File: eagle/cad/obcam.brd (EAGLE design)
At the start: 64 x 68 mm, 15 parts, among them IC1 NJM2391, IC2 TJ8S06M3L

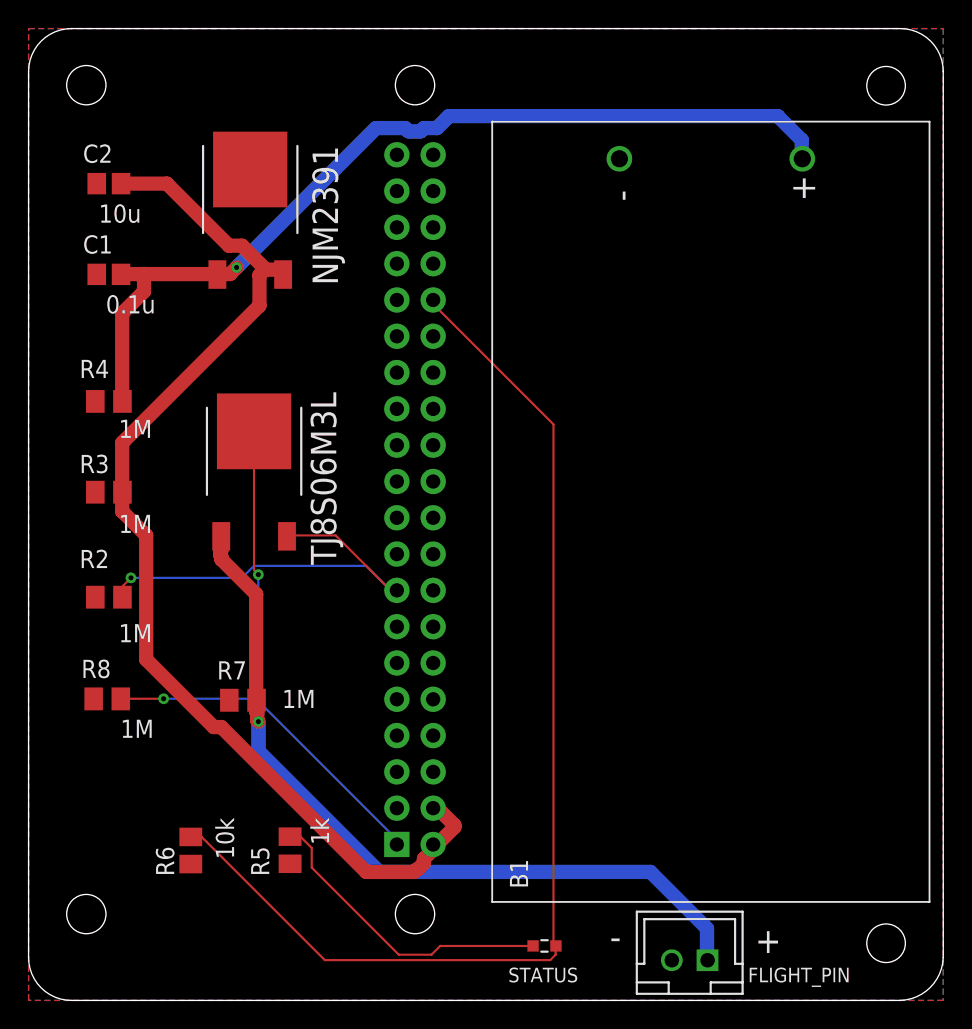
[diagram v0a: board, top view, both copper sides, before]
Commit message: Fixed the library of TJ8S06M3L and updated CAD.
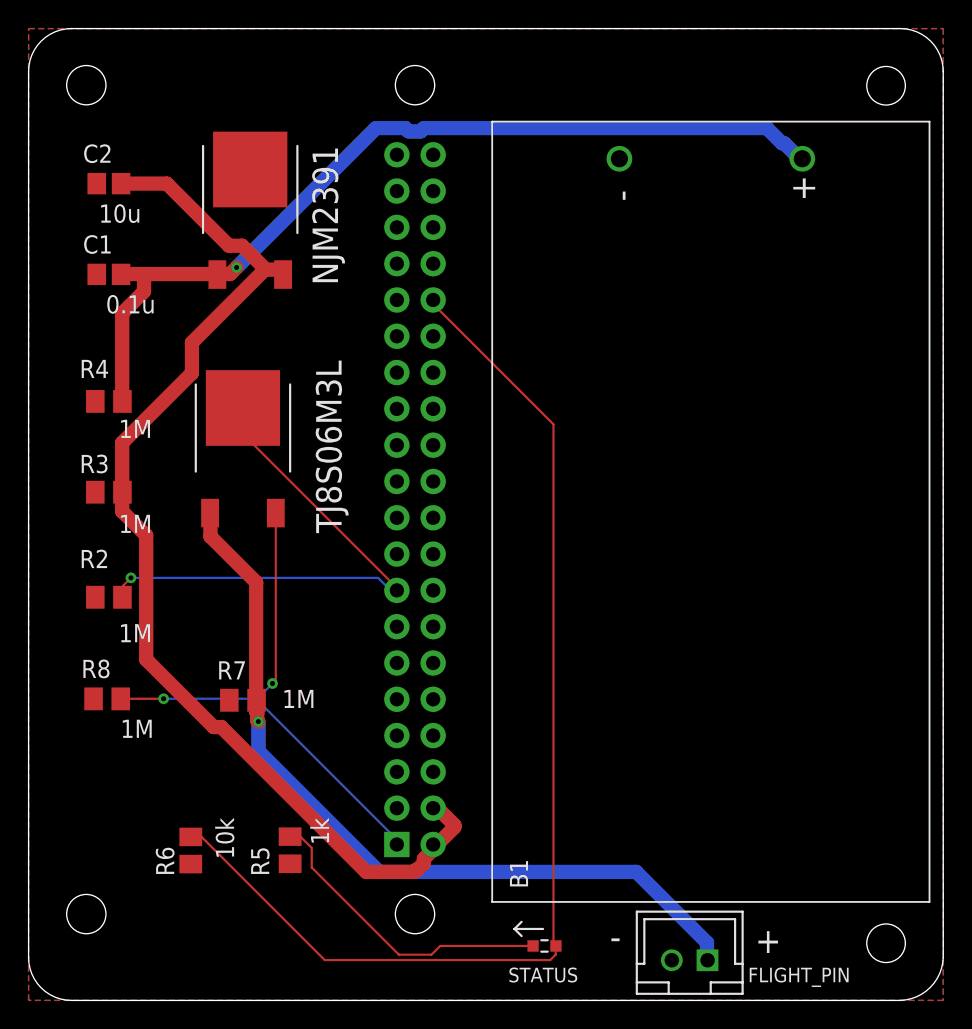
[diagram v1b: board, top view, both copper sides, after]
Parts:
- moved IC2 1.81 mm to (15.0, 37.0)
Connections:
- net 3V3@1: now also IC2.P$3; no longer IC2.P$2
- net FLIGHT_IO: now also IC2.P$2; no longer IC2.P$3
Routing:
- net FLIGHT_IO: track 30.6 -> 37.8 mm
- net 3V3@1: track 42.7 -> 37.3 mm
- net N$1: track 64.0 -> 62.6 mm
- net N$3: track 55.0 -> 56.3 mm
